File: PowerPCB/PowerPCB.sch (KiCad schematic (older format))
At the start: 28 parts, among them J1 Conn_01x03_Male, J2 Conn_01x10_Male, J3 STM Inputs, J4 STM Outputs, J5 Conn_01x07_Male, K1 1721081-5, K2 1721081-5, U1 NCP1117-3.3_SOT223, U2 STM32F413ZHTx, U3 NCP1117-5.0_SOT223, U4 MCP2562-E-P, U5 MCP2562-E-P

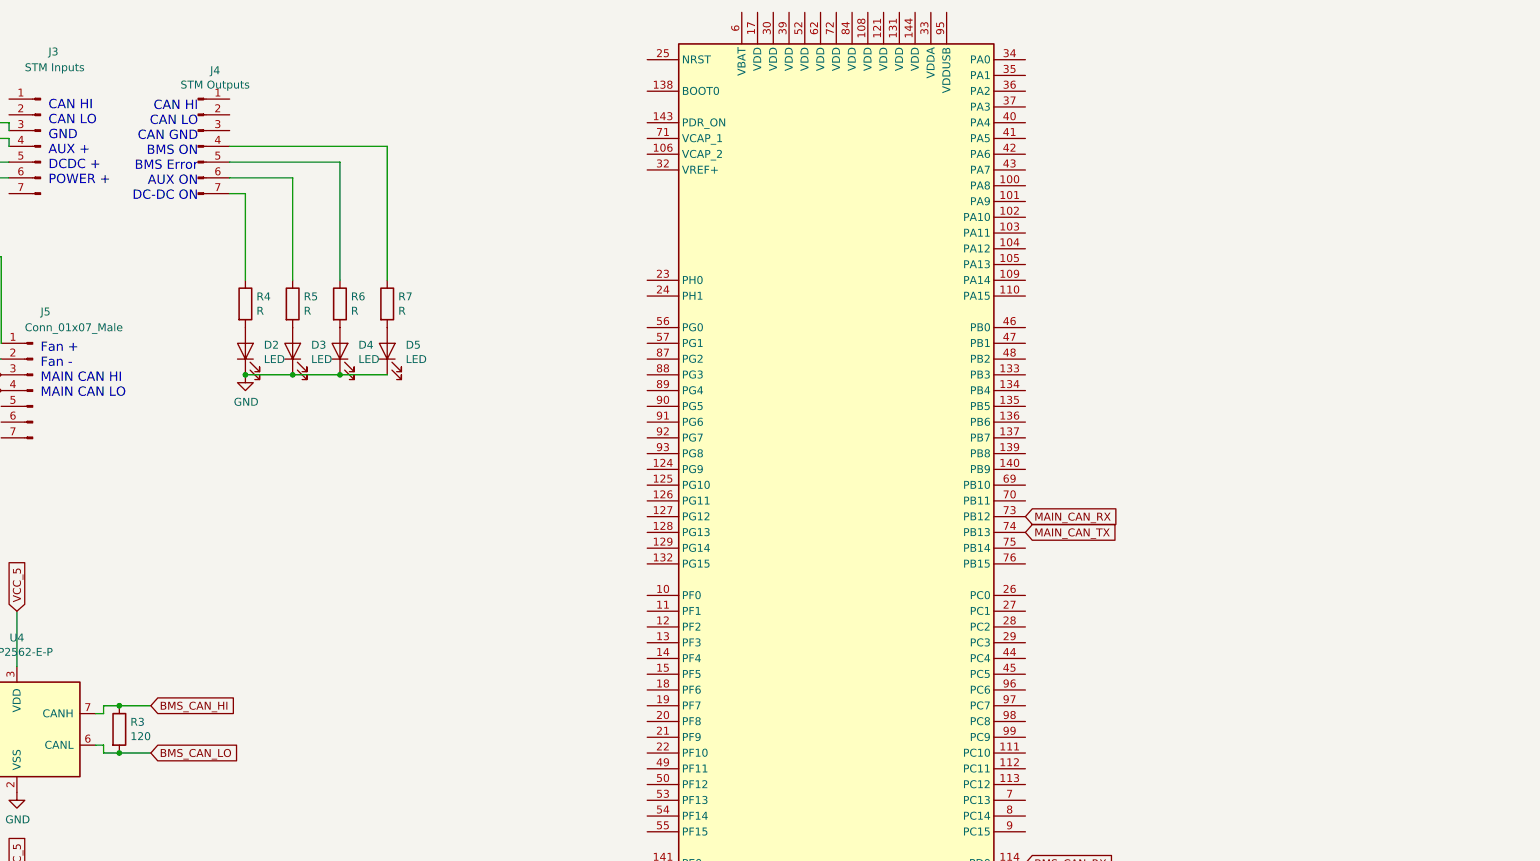
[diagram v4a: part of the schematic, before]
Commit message: Added LED connections to STM
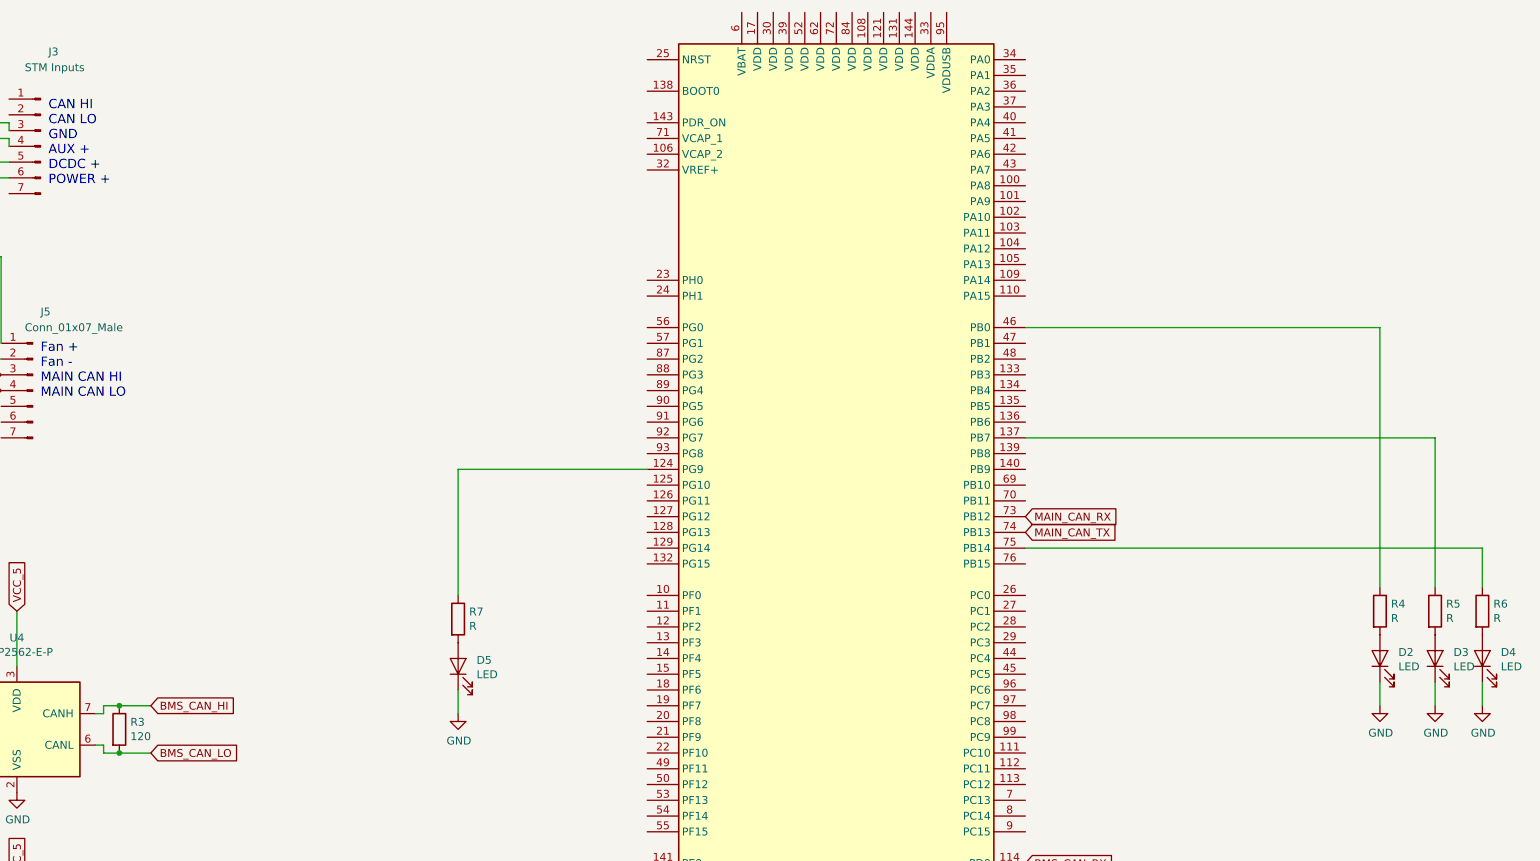
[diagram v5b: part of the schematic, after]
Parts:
- removed J4: STM Outputs, Connector_PinHeader_2.54mm:PinHeader_1x07_P2.54mm_Horizontal, symbol Connector:Conn_01x07_Male
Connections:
- net at R7.1: now also U2.124 (PG9)
- net at R6.1: now also U2.75 (PB14)
- net at R5.1: now also U2.137 (PB7)
- net at R4.1: now also U2.46 (PB0)
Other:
- note removed: "CAN HI\nCAN LO\nCAN GND\nBMS ON\nBMS Error\nAUX ON\nDC-DC ON"
- moved on the sheet: D2, D3, D4, D5, R4, R5, R6, R7
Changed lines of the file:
@@
 Wire Wire Line
 	5000 2050 4900 2050
-Wire Wire Line
-	7100 1950 7100 2700
-Wire Wire Line
-	6800 2700 6800 2050
-Wire Wire Line
-	7100 3300 6800 3300
-Connection ~ 7100 3300
-Connection ~ 6800 3300
 $Comp
 L Device:R R5
 U 1 1 5E984DE8
-P 6800 2850
-F 0 "R5" H 6870 2896 50  0000 L CNN
-F 1 "R" H 6870 2805 50  0000 L CNN
-F 2 "Resistor_SMD:R_0805_2012Metric_Pad1.15x1.40mm_HandSolder" V 6730 2850 50  0001 C CNN
-F 3 "~" H 6800 2850 50  0001 C CNN
-	1    6800 2850
+P 14050 4800
+F 0 "R5" H 14120 4846 50  0000 L CNN
+F 1 "R" H 14120 4755 50  0000 L CNN
+F 2 "Resistor_SMD:R_0805_2012Metric_Pad1.15x1.40mm_HandSolder" V 13980 4800 50  0001 C CNN
+F 3 "~" H 14050 4800 50  0001 C CNN
+	1    14050 4800
 	1    0    0    -1
 $EndComp
@@
 L Device:LED D3
 U 1 1 5E984DE2
-P 6800 3150
-F 0 "D3" V 6839 3033 50  0000 R CNN
-F 1 "LED" V 6748 3033 50  0000 R CNN
-F 2 "LED_SMD:LED_0805_2012Metric_Pad1.15x1.40mm_HandSolder" H 6800 3150 50  0001 C CNN
-F 3 "~" H 6800 3150 50  0001 C CNN
-	1    6800 3150
+P 14050 5100
+F 0 "D3" V 14089 4983 50  0000 R CNN
+F 1 "LED" V 13998 4983 50  0000 R CNN
+F 2 "LED_SMD:LED_0805_2012Metric_Pad1.15x1.40mm_HandSolder" H 14050 5100 50  0001 C CNN
+F 3 "~" H 14050 5100 50  0001 C CNN
+	1    14050 5100
 	0    -1   -1   0
 $EndComp
@@
 L Device:R R6
 U 1 1 5E980DA5
-P 7100 2850
-F 0 "R6" H 7170 2896 50  0000 L CNN
-F 1 "R" H 7170 2805 50  0000 L CNN
-F 2 "Resistor_SMD:R_0805_2012Metric_Pad1.15x1.40mm_HandSolder" V 7030 2850 50  0001 C CNN
-F 3 "~" H 7100 2850 50  0001 C CNN
-	1    7100 2850
+P 14350 4800
+F 0 "R6" H 14420 4846 50  0000 L CNN
+F 1 "R" H 14420 4755 50  0000 L CNN
+F 2 "Resistor_SMD:R_0805_2012Metric_Pad1.15x1.40mm_HandSolder" V 14280 4800 50  0001 C CNN
+F 3 "~" H 14350 4800 50  0001 C CNN
+	1    14350 4800
 	1    0    0    -1
 $EndComp
@@
 L Device:LED D4
 U 1 1 5E980D9F
-P 7100 3150
-F 0 "D4" V 7139 3033 50  0000 R CNN
-F 1 "LED" V 7048 3033 50  0000 R CNN
-F 2 "LED_SMD:LED_0805_2012Metric_Pad1.15x1.40mm_HandSolder" H 7100 3150 50  0001 C CNN
-F 3 "~" H 7100 3150 50  0001 C CNN
-	1    7100 3150
+P 14350 5100
+F 0 "D4" V 14389 4983 50  0000 R CNN
+F 1 "LED" V 14298 4983 50  0000 R CNN
+F 2 "LED_SMD:LED_0805_2012Metric_Pad1.15x1.40mm_HandSolder" H 14350 5100 50  0001 C CNN
+F 3 "~" H 14350 5100 50  0001 C CNN
+	1    14350 5100
 	0    -1   -1   0
 $EndComp
-Wire Wire Line
-	7400 2700 7400 1850
 $Comp
 L Device:R R7
 U 1 1 5E97E448
-P 7400 2850
-F 0 "R7" H 7470 2896 50  0000 L CNN
-F 1 "R" H 7470 2805 50  0000 L CNN
-F 2 "Resistor_SMD:R_0805_2012Metric_Pad1.15x1.40mm_HandSolder" V 7330 2850 50  0001 C CNN
-F 3 "~" H 7400 2850 50  0001 C CNN
-	1    7400 2850
-	1    0    0    -1
-$EndComp
-Wire Wire Line
-	7400 3300 7100 3300
+P 7850 4850
+F 0 "R7" H 7920 4896 50  0000 L CNN
+F 1 "R" H 7920 4805 50  0000 L CNN
+F 2 "Resistor_SMD:R_0805_2012Metric_Pad1.15x1.40mm_HandSolder" V 7780 4850 50  0001 C CNN
+F 3 "~" H 7850 4850 50  0001 C CNN
+	1    7850 4850
+	1    0    0    -1
+$EndComp
 $Comp
 L Device:LED D5
 U 1 1 5E979B1E
-P 7400 3150
-F 0 "D5" V 7439 3033 50  0000 R CNN
-F 1 "LED" V 7348 3033 50  0000 R CNN
-F 2 "LED_SMD:LED_0805_2012Metric_Pad1.15x1.40mm_HandSolder" H 7400 3150 50  0001 C CNN
-F 3 "~" H 7400 3150 50  0001 C CNN
-	1    7400 3150
+P 7850 5150
+F 0 "D5" V 7889 5033 50  0000 R CNN
+F 1 "LED" V 7798 5033 50  0000 R CNN
+F 2 "LED_SMD:LED_0805_2012Metric_Pad1.15x1.40mm_HandSolder" H 7850 5150 50  0001 C CNN
+F 3 "~" H 7850 5150 50  0001 C CNN
+	1    7850 5150
 	0    -1   -1   0
-$EndComp
-$Comp
-L Connector:Conn_01x07_Male J4
-U 1 1 5E97258B
-P 6200 1850
-F 0 "J4" H 6308 2331 50  0000 C CNN
-F 1 "STM Outputs" H 6308 2240 50  0000 C CNN
-F 2 "Connector_PinHeader_2.54mm:PinHeader_1x07_P2.54mm_Horizontal" H 6200 1850 50  0001 C CNN
-F 3 "~" H 6200 1850 50  0001 C CNN
-	1    6200 1850
-	1    0    0    -1
 $EndComp
 Wire Wire Line
@@
 	3150 1800 3250 1800
 Connection ~ 3250 1800
-Text Notes 6200 2200 2    59   ~ 0
-CAN HI\nCAN LO\nCAN GND\nBMS ON\nBMS Error\nAUX ON\nDC-DC ON
-Wire Wire Line
-	6400 2050 6800 2050
-Wire Wire Line
-	6400 1950 7100 1950
-Wire Wire Line
-	6400 1850 7400 1850
 $Comp
 L Device:R R4
 U 1 1 5EADC389
-P 6500 2850
-F 0 "R4" H 6570 2896 50  0000 L CNN
-F 1 "R" H 6570 2805 50  0000 L CNN
-F 2 "Resistor_SMD:R_0805_2012Metric_Pad1.15x1.40mm_HandSolder" V 6430 2850 50  0001 C CNN
-F 3 "~" H 6500 2850 50  0001 C CNN
-	1    6500 2850
+P 13700 4800
+F 0 "R4" H 13770 4846 50  0000 L CNN
+F 1 "R" H 13770 4755 50  0000 L CNN
+F 2 "Resistor_SMD:R_0805_2012Metric_Pad1.15x1.40mm_HandSolder" V 13630 4800 50  0001 C CNN
+F 3 "~" H 13700 4800 50  0001 C CNN
+	1    13700 4800
 	1    0    0    -1
 $EndComp
@@
 L Device:LED D2
 U 1 1 5EADC907
-P 6500 3150
-F 0 "D2" V 6539 3033 50  0000 R CNN
-F 1 "LED" V 6448 3033 50  0000 R CNN
-F 2 "LED_SMD:LED_0805_2012Metric_Pad1.15x1.40mm_HandSolder" H 6500 3150 50  0001 C CNN
-F 3 "~" H 6500 3150 50  0001 C CNN
-	1    6500 3150
+P 13700 5100
+F 0 "D2" V 13739 4983 50  0000 R CNN
+F 1 "LED" V 13648 4983 50  0000 R CNN
+F 2 "LED_SMD:LED_0805_2012Metric_Pad1.15x1.40mm_HandSolder" H 13700 5100 50  0001 C CNN
+F 3 "~" H 13700 5100 50  0001 C CNN
+	1    13700 5100
 	0    -1   -1   0
 $EndComp
-Wire Wire Line
-	6500 3300 6800 3300
-Wire Wire Line
-	6500 2700 6500 2150
-Wire Wire Line
-	6500 2150 6400 2150
 $Sheet
 S 4000 2450 750  300
@@
 L power:GND #PWR04
 U 1 1 5ED77241
-P 6500 3300
-F 0 "#PWR04" H 6500 3050 50  0001 C CNN
-F 1 "GND" H 6505 3127 50  0000 C CNN
-F 2 "" H 6500 3300 50  0001 C CNN
-F 3 "" H 6500 3300 50  0001 C CNN
-	1    6500 3300
-	1    0    0    -1
-$EndComp
-Connection ~ 6500 3300
+P 13700 5400
+F 0 "#PWR04" H 13700 5150 50  0001 C CNN
+F 1 "GND" H 13705 5227 50  0000 C CNN
+F 2 "" H 13700 5400 50  0001 C CNN
+F 3 "" H 13700 5400 50  0001 C CNN
+	1    13700 5400
+	1    0    0    -1
+$EndComp
 Text GLabel 4900 2050 0    50   Input ~ 0
 VCC_3.3
@@
 Text GLabel 11450 4200 2    50   Input ~ 0
 MAIN_CAN_RX
+Wire Wire Line
+	13700 5400 13700 5250
+$Comp
+L power:GND #PWR?
+U 1 1 5EE1DD69
+P 14050 5400
+F 0 "#PWR?" H 14050 5150 50  0001 C CNN
+F 1 "GND" H 14055 5227 50  0000 C CNN
+F 2 "" H 14050 5400 50  0001 C CNN
+F 3 "" H 14050 5400 50  0001 C CNN
+	1    14050 5400
+	1    0    0    -1
+$EndComp
+Wire Wire Line
+	14050 5400 14050 5250
+$Comp
+L power:GND #PWR?
+U 1 1 5EE1FD63
+P 14350 5400
+F 0 "#PWR?" H 14350 5150 50  0001 C CNN
+F 1 "GND" H 14355 5227 50  0000 C CNN
+F 2 "" H 14350 5400 50  0001 C CNN
+F 3 "" H 14350 5400 50  0001 C CNN
+	1    14350 5400
+	1    0    0    -1
+$EndComp
+Wire Wire Line
+	14350 5400 14350 5250
+$Comp
+L power:GND #PWR?
+U 1 1 5EE21DB4
+P 7850 5450
+F 0 "#PWR?" H 7850 5200 50  0001 C CNN
+F 1 "GND" H 7855 5277 50  0000 C CNN
+F 2 "" H 7850 5450 50  0001 C CNN
+F 3 "" H 7850 5450 50  0001 C CNN
+	1    7850 5450
+	1    0    0    -1
+$EndComp
+Wire Wire Line
+	7850 5450 7850 5300
+Wire Wire Line
+	13700 4650 13700 3000
+Wire Wire Line
+	13700 3000 11450 3000
+Wire Wire Line
+	14050 4650 14050 3700
+Wire Wire Line
+	14050 3700 11450 3700
+Wire Wire Line
+	14350 4650 14350 4400
+Wire Wire Line
+	14350 4400 11450 4400
+Wire Wire Line
+	7850 3900 9050 3900
+Wire Wire Line
+	7850 3900 7850 4700
 $EndSCHEMATC

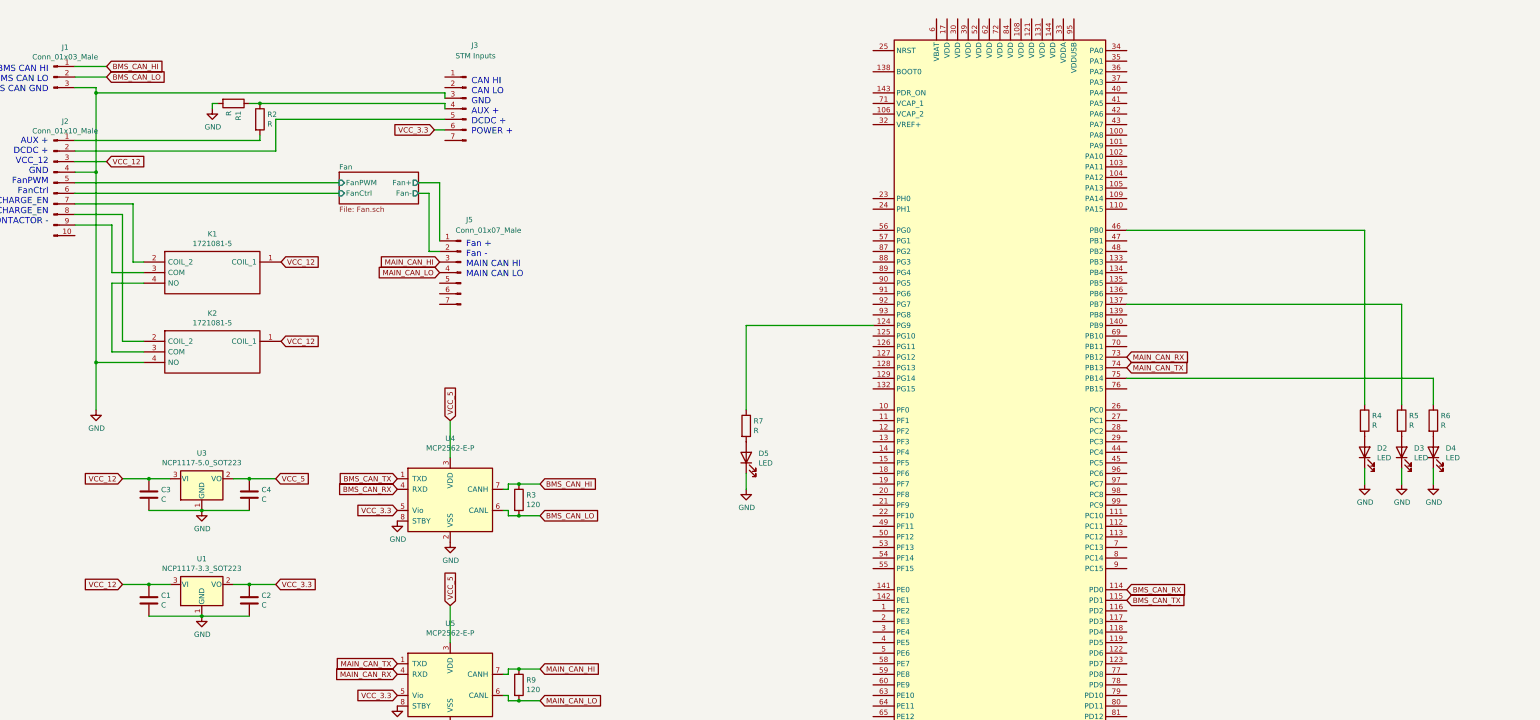
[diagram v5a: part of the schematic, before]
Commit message: Added AUX+ and DCDC+ as analog inputs
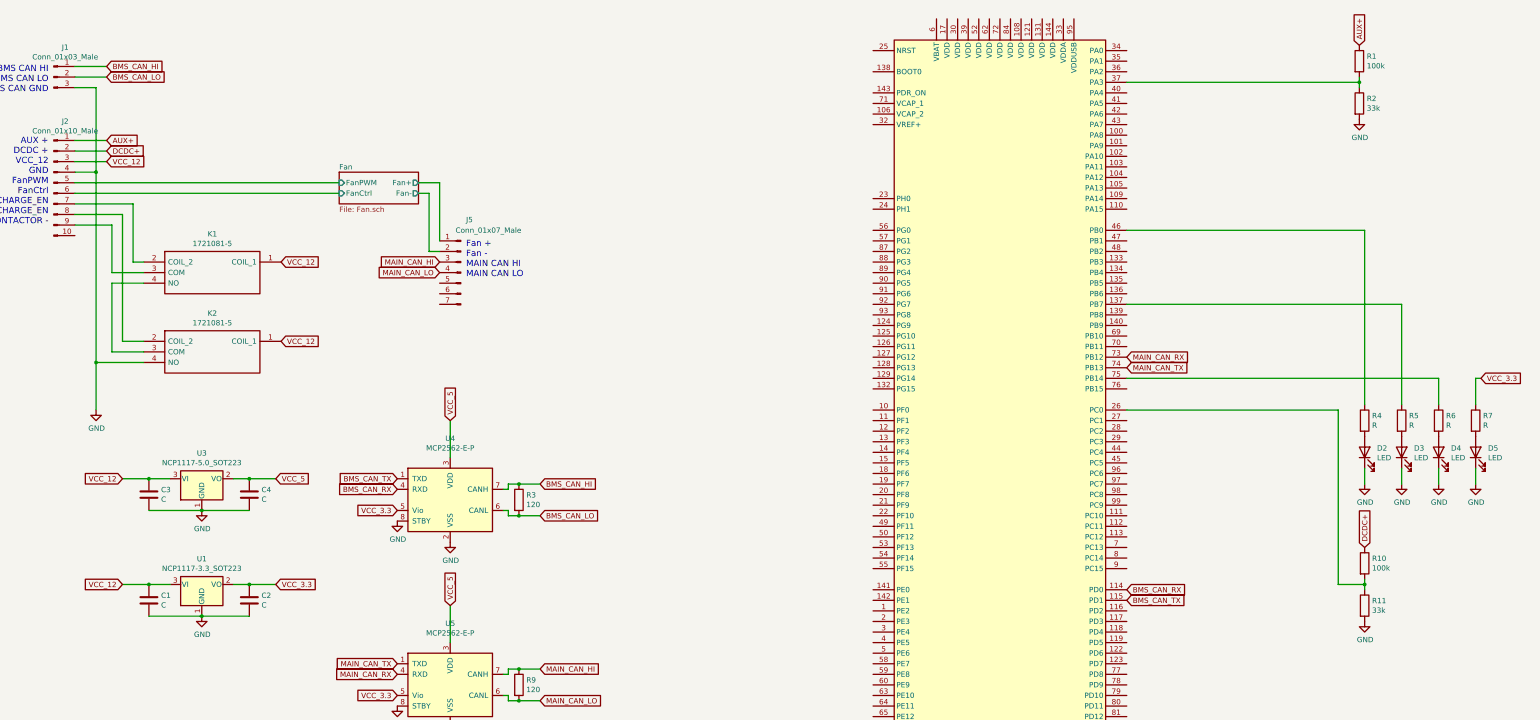
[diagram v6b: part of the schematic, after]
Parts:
- removed J3: STM Inputs, Connector_PinHeader_2.54mm:PinHeader_1x07_P2.54mm_Horizontal, symbol Connector:Conn_01x07_Male
- added R10: 100k, Resistor_SMD:R_0805_2012Metric_Pad1.15x1.40mm_HandSolder, symbol Device:R
- added R11: 33k, Resistor_SMD:R_0805_2012Metric_Pad1.15x1.40mm_HandSolder, symbol Device:R
- R1: value R -> 100k
- R2: value R -> 33k
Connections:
- net GND: now also R2.2, R11.2; no longer R1.2
- net VCC_3.3: now also R7.1
- net at R2.1: now also R1.2, U2.37 (PA3); no longer R1.1
- net DCDC+: now reaches J2.2 (Pin_2)
- net DCDC+: now also R10.1
- net at U2.124 (PG9): no longer R7.1
- net AUX+: now reaches J2.1 (Pin_1)
- net AUX+: now also R1.1; no longer R2.2
- net at U2.26 (PC0): now also R10.2, R11.1
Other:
- note removed: "CAN HI\nCAN LO\nGND\nAUX +\nDCDC +\nPOWER +"
- moved on the sheet: D4, D5, R1, R2, R6, R7

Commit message: Finished connections to STM, exported to PCBnew
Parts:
- added C5: C, Capacitor_SMD:C_0805_2012Metric_Pad1.15x1.40mm_HandSolder, symbol Device:C
- added C6, C7: 2.2u, Capacitor_SMD:C_0805_2012Metric_Pad1.15x1.40mm_HandSolder, symbol Device:C
- added C8: 100n, Capacitor_SMD:C_0805_2012Metric_Pad1.15x1.40mm_HandSolder, symbol Device:C
- added D1: LED, LED_SMD:LED_0805_2012Metric_Pad1.15x1.40mm_HandSolder, symbol Device:LED
- added R12, R13: 100k, Resistor_SMD:R_0805_2012Metric_Pad1.15x1.40mm_HandSolder, symbol Device:R
- added R14: 33k, Resistor_SMD:R_0805_2012Metric_Pad1.15x1.40mm_HandSolder, symbol Device:R
- added R15: R, Resistor_SMD:R_0805_2012Metric_Pad1.15x1.40mm_HandSolder, symbol Device:R
- added R16: 40k, Resistor_SMD:R_0805_2012Metric_Pad1.15x1.40mm_HandSolder, symbol Device:R
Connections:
- net AUX+: now also J2.2 (Pin_2); no longer J2.1 (Pin_1)
- net DCDC+: now also J2.3 (Pin_3); no longer J2.2 (Pin_2)
- net Fan/FanCtrl: now also J2.7 (Pin_7); no longer J2.6 (Pin_6)
- net Fan/FanPWM: now also J2.6 (Pin_6); no longer J2.5 (Pin_5)
- net GND: now also J2.5 (Pin_5), U2.107 (VSS), U2.120 (VSS), U2.130 (VSS), U2.138 (BOOT0), U2.16 (VSS), U2.31 (VSSA), U2.38 (VSS), U2.51 (VSS), U2.61 (VSS), U2.83 (VSS), U2.94 (VSS), C5.2, C6.2, C7.2, C8.2, D1.1 (K), R12.2, R14.2; no longer J2.4 (Pin_4)
- net VCC_12: now also J2.4 (Pin_4); no longer J2.3 (Pin_3)
- net VCC_3.3: now also U2.108 (VDD), U2.121 (VDD), U2.131 (VDD), U2.143 (PDR_ON), U2.144 (VDD), U2.17 (VDD), U2.30 (VDD), U2.32 (VREF+), U2.33 (VDDA), U2.39 (VDD), U2.52 (VDD), U2.6 (VBAT), U2.62 (VDD), U2.72 (VDD), U2.84 (VDD), C5.1, C8.1, R16.1
- net at U2.106 (VCAP_2): now also C6.1
- net at U2.124 (PG9): now also R13.2, R14.1
- net at U2.25 (NRST): now also R16.2
- net at U2.71 (VCAP_1): now also C7.1
- net at J2.10 (Pin_10): now also K1.3 (COM)
- net at K1.2 (COIL_2): now also J2.8 (Pin_8); no longer J2.7 (Pin_7)
- net at K2.2 (COIL_2): now also J2.9 (Pin_9); no longer J2.8 (Pin_8)
- new net: D1.2 (A), R15.2
- new net DCDC_ON: J2.1 (Pin_1), R12.1, R13.1, R15.1
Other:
- note added: "DCDC ON\nAUX +\nDCDC +\nVCC_12\nGND\nFanPWM\nFanCtrl\nDISCHARGE_EN\nCHARGE_EN\nCONTACTOR -"
- note removed: "AUX +\nDCDC +\nVCC_12\nGND\nFanPWM\nFanCtrl\nDISCHARGE_EN\nCHARGE_EN\nCONTACTOR -"
- moved on the sheet: D2, D3, D4, D5, J2, R1, R10, R11, R2, R4, R5, R6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
